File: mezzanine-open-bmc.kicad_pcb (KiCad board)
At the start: 2 copper layers, 85 x 54.1 mm, 50 parts, among them P1 CONN_02X20, P2 CONN_02X20, Q1 S8050, Q2 S8050, SW1 PWR, SW2 RST, U1 FT230XS, U2 PMIC-CJT1117-3.3(SOT223), U4 PCA9306, U5 M24C16-WMN6P

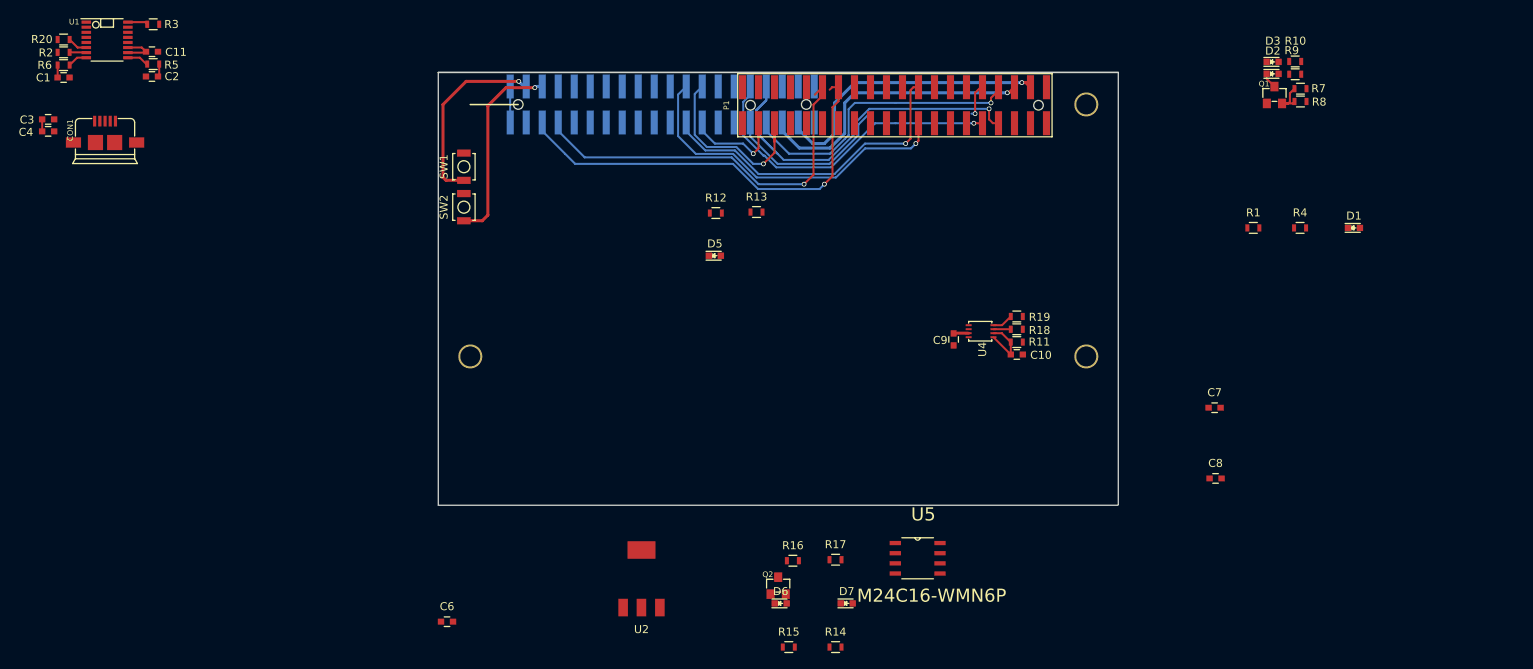
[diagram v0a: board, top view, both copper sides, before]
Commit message: Wire Up BMC LED's
The wiring for the BMC PWR LED's have been connnected up in a neat
little bundle which can be placed on the board.

Signed-off-by: Sophie Haynes <sophie.haynes@linaro.org>
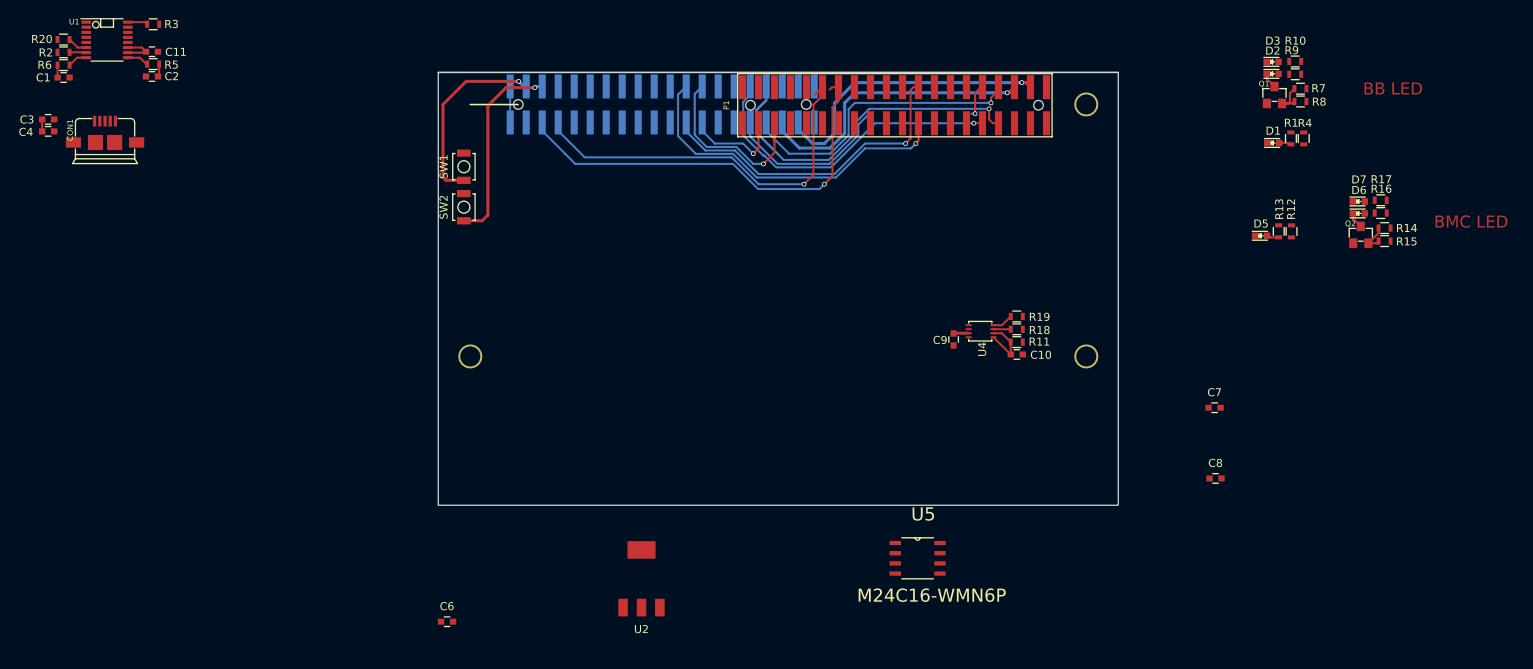
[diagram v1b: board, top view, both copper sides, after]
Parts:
- moved R15 90.1 mm to (218.3, 121.1)
- moved D6 87.2 mm to (215.1, 117.6)
- moved R14 86.3 mm to (218.3, 119.5)
- moved R16 85.4 mm to (217.8, 117.6)
- moved Q2 85.0 mm to (215.3, 120.3)
- moved R17 81.6 mm to (217.8, 116.0)
- moved D7 81.4 mm to (215.1, 116.1)
- moved R12 72.0 mm to (206.7, 119.9), turned to 270 degrees
- moved D5 68.3 mm to (202.8, 120.4)
- moved R13 65.3 mm to (205.1, 119.9), turned to 270 degrees
- moved D1 14.6 mm to (204.4, 108.8)
- moved R1 12.1 mm to (206.6, 108.3), turned to 270 degrees
- moved R4 11.2 mm to (208.2, 108.3), turned to 270 degrees
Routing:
- net Net-(Q2-Pad2): track 0.00 -> 3.81 mm
- net Net-(D6-Pad1): track 0.00 -> 2.02 mm
- net Net-(D1-Pad2): track 0.00 -> 1.54 mm
- net Net-(D5-Pad2): track 0.00 -> 1.54 mm
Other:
- board text added: "BB LED"
- board text added: "BMC LED"

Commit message: Start Track Layout
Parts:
- U2: footprint 96boards:SOT-223 -> 96boards:SOT-223(PMIC)
- moved R20 75.4 mm to (122.5, 125.3), turned to 180 degrees
- moved R2 74.2 mm to (122.5, 123.7), turned to 180 degrees
- moved R4 73.6 mm to (135.0, 116.2), turned to 180 degrees
- moved R6 73.1 mm to (122.5, 122.1), turned to 0 degrees
- moved C1 72.2 mm to (122.5, 120.6), turned to 180 degrees
- moved R1 71.8 mm to (135.0, 114.6), turned to 180 degrees
- moved D1 69.4 mm to (135.1, 113.0), turned to 180 degrees
- moved C4 68.0 mm to (117.9, 120.5), turned to 90 degrees
- moved D2 67.9 mm to (137.9, 114.5)
- moved D3 67.9 mm to (137.9, 113.0)
- moved Q1 67.9 mm to (138.2, 117.2)
- moved R10 67.9 mm to (140.8, 113.0)
- moved R9 67.9 mm to (140.8, 114.6)
- moved R7 67.9 mm to (141.4, 116.4)
- moved R8 67.9 mm to (141.4, 118.0)
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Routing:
- net Net-(C1-Pad1): track 1.55 -> 26.2 mm
- net GPIO_F_BMC: track 0.00 -> 21.6 mm, vias 0 -> 1
- net VBUS: track 1.50 -> 16.2 mm
- net RST_BTN_BMC: track 24.7 -> 36.9 mm, vias 1 -> 3
- net GPIO_E_BMC: track 0.00 -> 11.3 mm, vias 0 -> 1
- net Net-(C2-Pad1): track 1.61 -> 10.8 mm
- net +1V8: track 38.3 -> 47.3 mm, vias 1 -> 2
- net GPIO_L: track 54.2 -> 50.5 mm
- net SYS_DCIN: track 0.00 -> 2.00 mm
- net +5V: track 37.5 -> 39.1 mm
- net UART0_RX_BMC: track 49.0 -> 50.4 mm
- net Net-(D2-Pad2): track 0.00 -> 1.34 mm
- net Net-(D3-Pad2): track 0.00 -> 1.34 mm
- net GPIO_C_BMC: track 14.5 -> 15.3 mm

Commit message: Grant Tweaks
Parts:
- removed D2, D6: Led_Small, LEDs:LED_0603
- removed Q1, Q2: S8050, 96boards:SOT-23_Seeed
- removed R12: 22R, Resistors_SMD:R_0603
- removed R14: 1k, Resistors_SMD:R_0603
- removed R15: 10k, Resistors_SMD:R_0603
- removed R16, R9: 390R, Resistors_SMD:R_0603
- added C5: 33u, Capacitors_SMD:C_0603, F.Cu at (142.5, 164.2)
- added U3: DS3231N, SMD_Packages:SO-16-W, F.Cu at (142.5, 164.2)
- R18, R19: value 2.2K Ω -> 2.2K
- R4: value 22R -> 10k
- R5, R6: value 220R -> 22R
- R7: value 1k -> 0R
- R8: value 10k -> 0R
- U2: footprint 96boards:SOT-223(PMIC) -> TO_SOT_Packages_SMD:SOT-223
- moved R17 80.4 mm to (137.9, 125.3), turned to 270 degrees
- moved D7 77.9 mm to (138.1, 128.1), turned to 90 degrees
- moved C7 61.9 mm to (135.3, 146.8)
- moved U5 48.8 mm to (152.1, 112.5), turned to 90 degrees
- moved C6 46.9 mm to (139.2, 141.2)
- moved D5 31.5 mm to (171.3, 120.0)
- moved R13 31.5 mm to (173.6, 119.5)
- moved U2 24.3 mm to (151.2, 141.4)
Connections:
- net UART0_CTS_BMC renamed Net-(P2-Pad3)
- net UART0_RTS_BMC renamed Net-(P2-Pad9)
- net UART0_RX_BMC renamed UART1_TX
- net UART0_TX_BMC renamed UART1_RX
- C6 pad 1: Net-(C6-Pad1) -> GND
- C6 pad 2: GND -> +5V
- P1 pad 4: GPIO_C_BMC -> PWR_BTN_N
- P1 pad 6: GPIO_D_BMC -> RST_BTN_N
- R18 pad 1: I2C0_SCL_3.3 -> +3V3
- R18 pad 2: Net-(R18-Pad2) -> I2C0_SDA_3.3
- R19 pad 1: I2C0_SDA_3.3 -> I2C0_SCL_3.3
- R19 pad 2: Net-(R19-Pad2) -> +3V3
- R4 pad 1: +5V -> +1V8
- R7 pad 1: Net-(Q1-Pad2) -> GPIO_C_BMC
- R7 pad 2: GPIO_F_BMC -> PWR_BTN_N
- R8 pad 1: Net-(Q1-Pad2) -> GPIO_D_BMC
- R8 pad 2: GND -> RST_BTN_N
- U2 pad 1: Net-(C6-Pad1) -> GND
- U2 pad 2: GND -> +3V3
- U2 pad 3: GND -> +5V
- U4 pad 5: Net-(C10-Pad1) -> I2C0_SDA_3.3
- U4 pad 6: Net-(C10-Pad1) -> I2C0_SCL_3.3
- U4 pad 7: Net-(R18-Pad2) -> Net-(C10-Pad1)
- U4 pad 8: Net-(R19-Pad2) -> Net-(C10-Pad1)
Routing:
- net (no net): track 0.00 -> 10.4 mm
- net I2C0_SDA: track 0.00 -> 8.59 mm
- net I2C0_SCL: track 0.00 -> 8.22 mm
- net PWR_BTN_N: track 0.00 -> 7.39 mm
- net RST_BTN_N: track 0.00 -> 5.45 mm
- net Net-(Q1-Pad2): track 4.60 -> 0.00 mm
- net Net-(Q2-Pad2): track 3.81 -> 0.00 mm
- net GPIO_D_BMC: track 24.2 -> 20.4 mm
- net GPIO_F_BMC: track 21.6 -> 18.2 mm
- net I2C0_SDA_3.3: track 0.00 -> 3.07 mm
- net Net-(R19-Pad2): track 2.62 -> 0.00 mm
- net Net-(R18-Pad2): track 2.17 -> 0.00 mm
- net Net-(D6-Pad1): track 2.02 -> 0.00 mm
- net Net-(D2-Pad1): track 1.99 -> 0.00 mm
- net +3V3: track 0.00 -> 1.54 mm
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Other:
- board text removed: "BB LED"
- board text removed: "BMC LED"

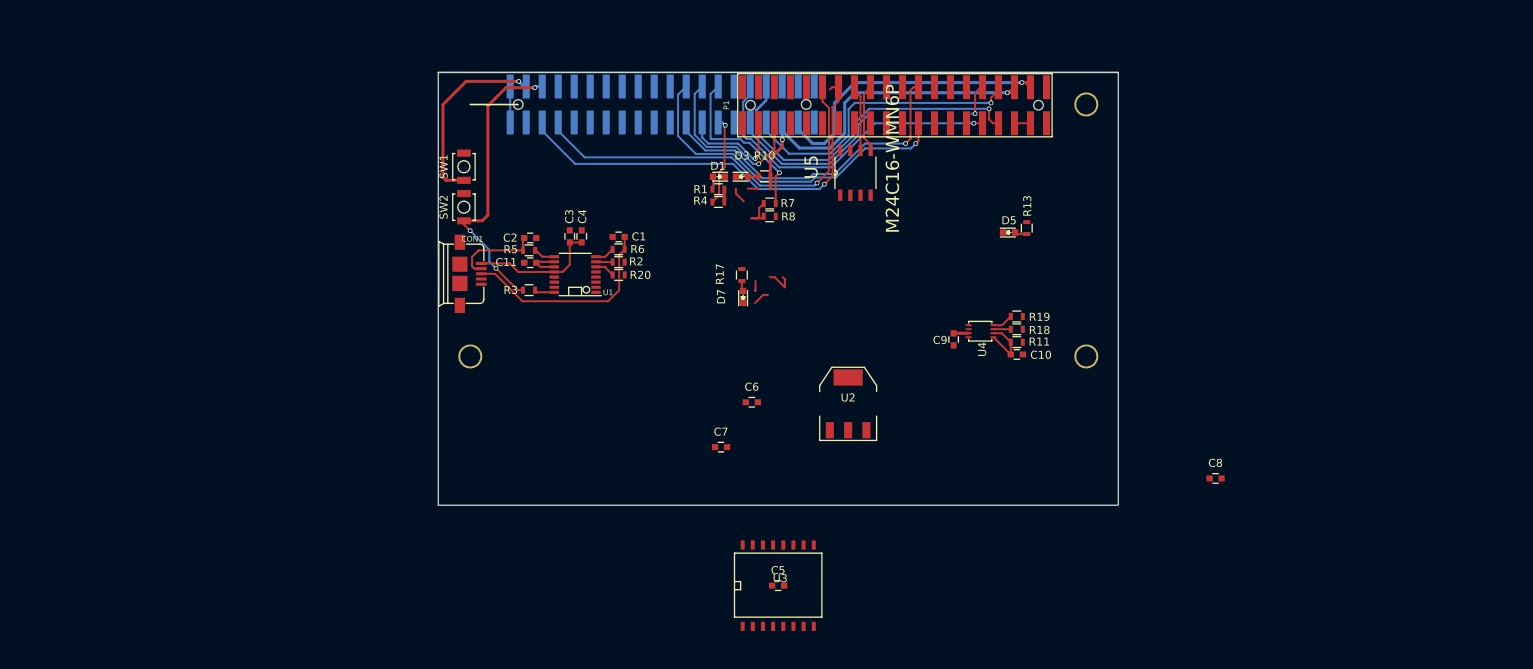
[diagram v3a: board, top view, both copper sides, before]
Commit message: Connect Up Components
All components are connected (barring the battery since there is no
footprint currently)

Signed-off-by: Sophie Haynes <sophie.haynes@linaro.com>
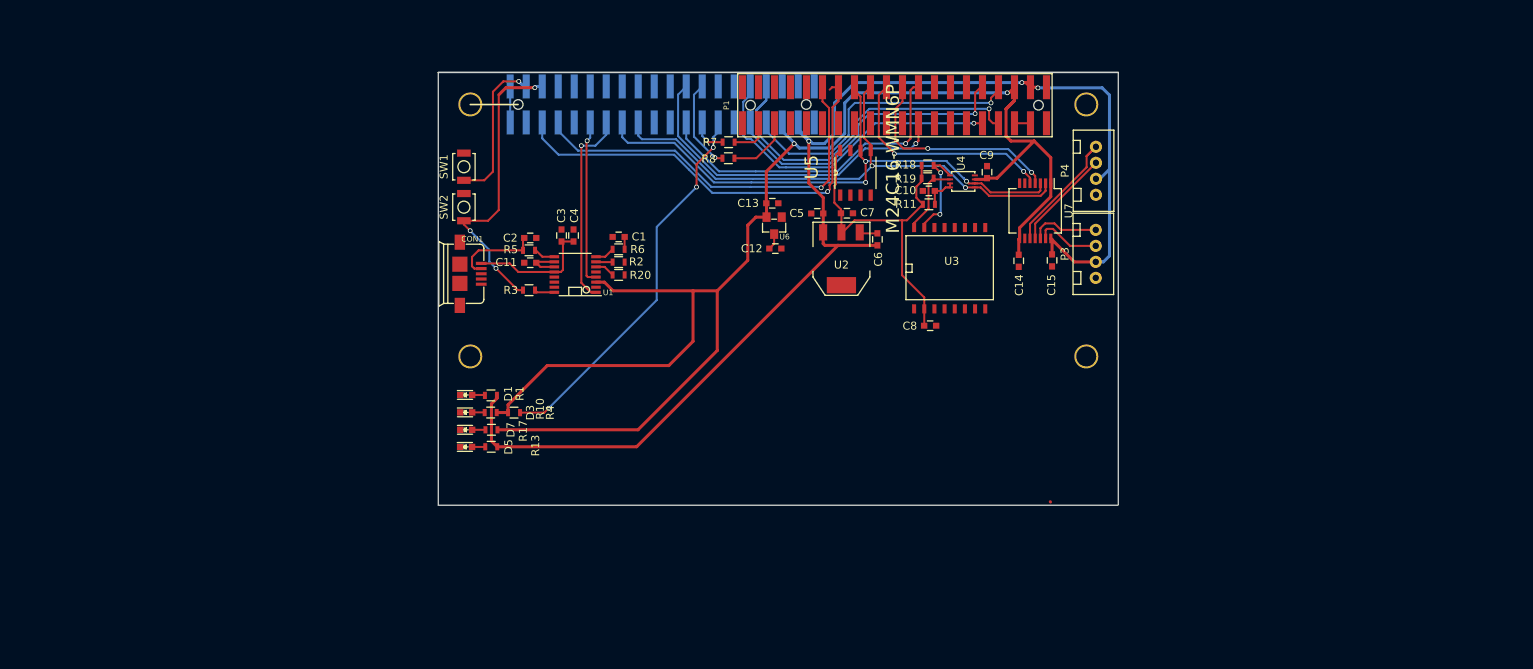
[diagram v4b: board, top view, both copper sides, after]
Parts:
- added C12: 1uF, Capacitors_SMD:C_0603, F.Cu at (142.1, 122.0)
- added C13: 1uF, Capacitors_SMD:C_0603, F.Cu at (141.8, 116.4)
- added C14: 100n, Capacitors_SMD:C_0603, F.Cu at (172.6, 123.5)
- added C15: 100n, Capacitors_SMD:C_0603, F.Cu at (176.7, 123.5)
- added P3: CONN_01X04, 96boards:Grove4P, F.Cu at (184.7, 122.7)
- added P4: CONN_01X04, 96boards:Grove4P, F.Cu at (184.7, 112.3)
- added REF**: Hole_2.5MM, Sensors:Hole_2.5MM, F.Cu at (104.0, 103.9)
- added U6: REG_1.8V, 96boards:SOT-23_Seeed, F.Cu at (142.0, 119.1)
- added U7: TXS0104PW, Housings_SSOP:SSOP-14_5.3x6.2mm_Pitch0.65mm, F.Cu at (174.6, 117.3)
- U2: value PMIC-CJT1117-3.3(SOT223) -> SOT223
- moved D5 73.0 mm to (103.5, 146.8)
- moved R13 72.3 mm to (106.6, 146.8), turned to 180 degrees
- moved C5 46.8 mm to (147.4, 117.6), turned to 180 degrees
- moved D3 45.3 mm to (103.5, 142.5)
- moved R10 45.2 mm to (106.5, 142.5)
- moved U3 45.1 mm to (163.9, 124.5)
- moved D1 41.7 mm to (103.5, 140.3), turned to 0 degrees
- moved C8 40.5 mm to (161.5, 131.7)
- moved D7 38.4 mm to (103.5, 144.7), turned to 0 degrees
- moved R1 38.4 mm to (106.6, 140.4)
- moved R17 36.8 mm to (106.6, 144.7), turned to 180 degrees
- moved R4 36.7 mm to (109.5, 142.5), turned to 0 degrees
- moved C7 33.2 mm to (151.1, 117.6)
- moved C6 25.7 mm to (154.9, 120.9), turned to 270 degrees
- moved R18 23.3 mm to (161.2, 111.6), turned to 0 degrees
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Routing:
- net +1V8: track 47.3 -> 187.7 mm
- net +5V: track 39.1 -> 165.2 mm, vias 1 -> 3
- net I2C0_SCL: track 8.22 -> 72.4 mm, vias 0 -> 3
- net I2C0_SDA: track 8.59 -> 68.8 mm, vias 0 -> 2
- net +3V3: track 1.54 -> 42.6 mm
- net GPIO_E_BMC: track 11.3 -> 48.3 mm, vias 1 -> 3
- net I2C1_SCL: track 0.00 -> 28.4 mm, vias 0 -> 2
- net I2C1_SDA: track 0.00 -> 27.3 mm, vias 0 -> 2
- net UART1_RX_BMC: track 0.00 -> 26.2 mm, vias 0 -> 1
- net Net-(C1-Pad1): track 26.2 -> 1.55 mm
- net UART1_TX_BMC: track 0.00 -> 20.6 mm, vias 0 -> 1
- net GPIO_F_BMC: track 18.2 -> 0.30 mm, vias 1 -> 0
- net I2C1_SCL/5: track 0.00 -> 16.5 mm
- net GPIO_I: track 25.4 -> 38.2 mm
- net I2C1_SDA/5: track 0.00 -> 12.6 mm
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
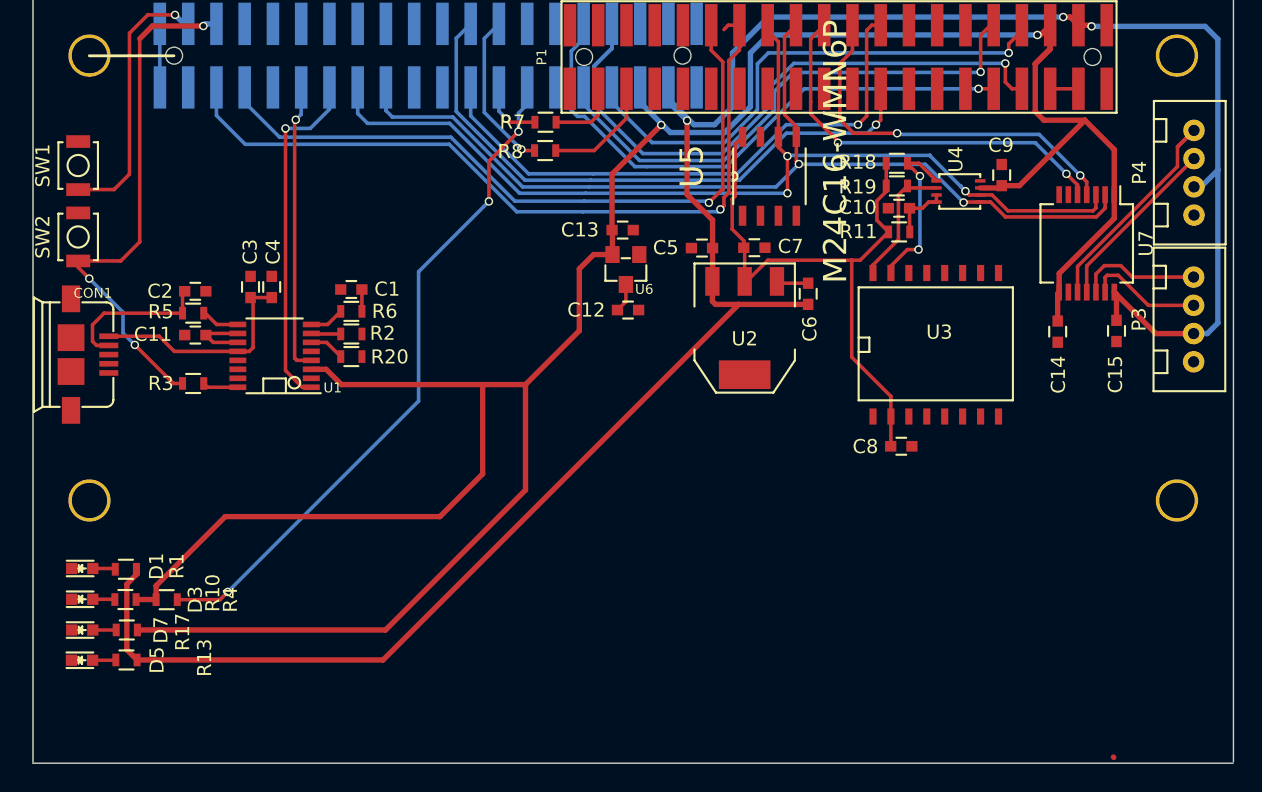
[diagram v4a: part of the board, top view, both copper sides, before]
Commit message: Complete PCB Layout and Include Missing Footprints (BT1, C5, C7)
The missing footprints have been added to both the schematic and the PCB.
Capacitor values for C6 have been changes to 0.1uF.
The new components have been connected up in the PCB.

Signed-off-by: Sophie Haynes <sophie.haynes@linaro.org>
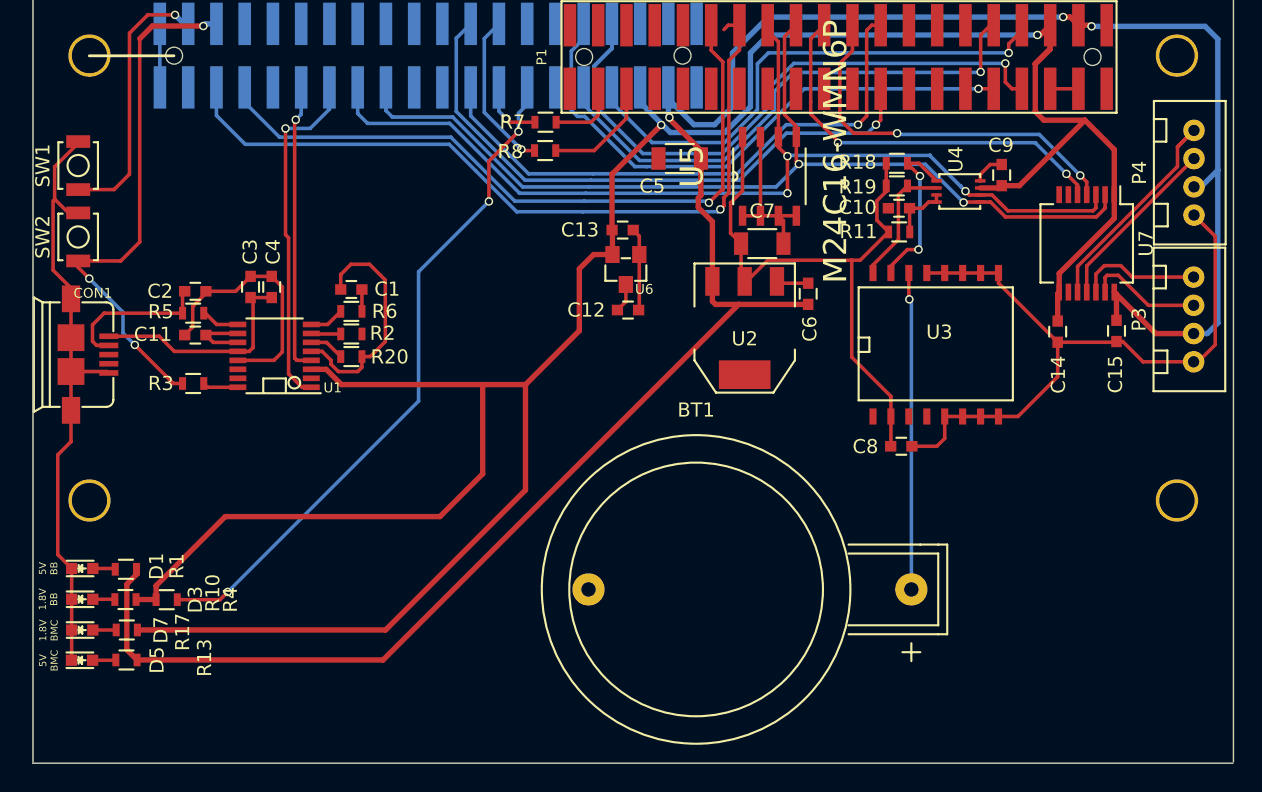
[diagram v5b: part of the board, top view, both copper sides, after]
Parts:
- added BT1: Battery CR2032, Connect:CR2032H, F.Cu at (147.0, 141.8)
- C5, C7: footprint Capacitors_SMD:C_0603 -> Capacitors_SMD:C_1206
- C6: value 0.47u -> 0.1u
- moved C5 6.53 mm to (145.8, 111.3)
- moved C7 0.63 mm to (151.6, 117.3)
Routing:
- net GND: track 6.77 -> 153.9 mm
- net Net-(BT1-Pad1): track 0.00 -> 22.5 mm, vias 0 -> 1
- net +5V: track 165.2 -> 166.3 mm
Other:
- board text added: "1.8V BB"
- board text added: "1.8V BMC"
- board text added: "5V BB"
- board text added: "5V BMC"
